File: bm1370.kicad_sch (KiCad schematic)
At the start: 48 parts, among them U5 MCP1824T-1202E/OT, U6 MCP1824T-0802E, U7 25MHz, U8 BM1370_mode1, U9 SN74AVC4T774

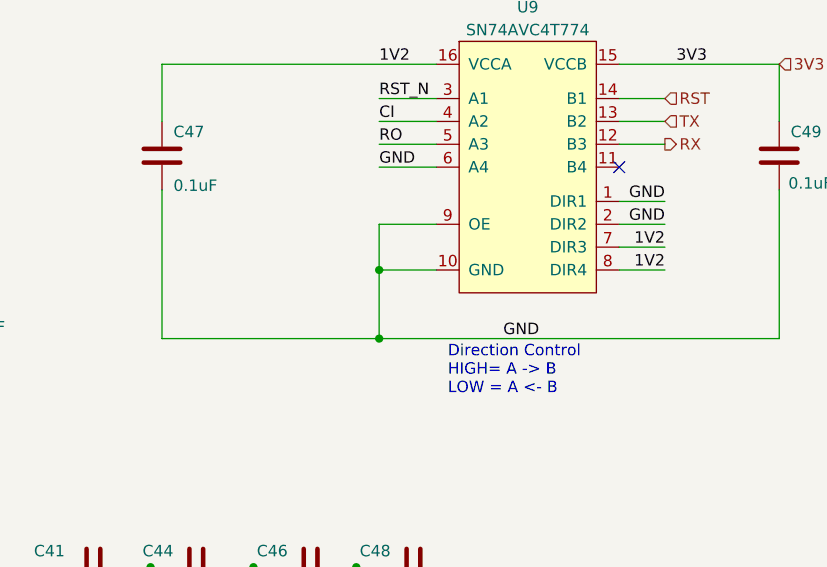
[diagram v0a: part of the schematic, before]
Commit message: Revert "bump version to 602. remove R21 and fix for #6"
This reverts commit 8bd74c865f9910776743c8aa45b35babe35214af.
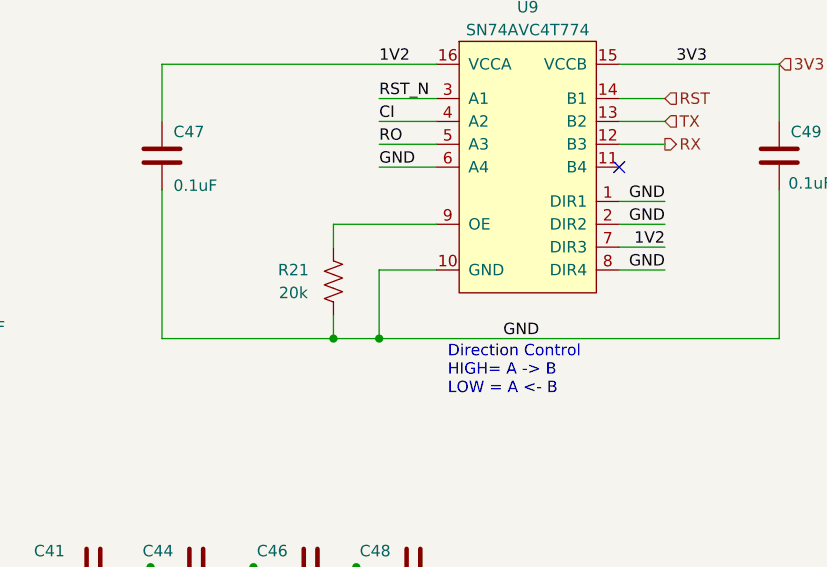
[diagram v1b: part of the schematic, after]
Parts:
- added R21: 20k, Resistor_SMD:R_0402_1005Metric, symbol Device:R_US
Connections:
- net 1V2: no longer U9.8 (DIR4)
- net GND: now also U9.8 (DIR4), R21.1; no longer U9.9 (OE)
- new net: R21.2, U9.9 (OE)
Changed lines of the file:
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@@
 	(title_block
 		(title "bitaxeGamma")
-		(date "2024-09-26")
-		(rev "602")
+		(date "2024-08-16")
+		(rev "600")
 	)
 	(junction
@@
 	)
 	(junction
-		(at 198.12 52.07)
-		(diameter 0)
-		(color 0 0 0 0)
-	)
-	(junction
 		(at 198.12 59.69)
 		(diameter 0)
@@
 	)
 	(junction
+		(at 193.04 59.69)
+		(diameter 0)
+		(color 0 0 0 0)
+	)
+	(junction
 		(at 140.97 85.09)
 		(diameter 0)
@@
 	(wire
 		(pts
-			(xy 242.57 43.18) (xy 242.57 59.69)
+			(xy 193.04 59.69) (xy 193.04 57.15)
 		)
 		(stroke
@@
 	(wire
 		(pts
-			(xy 180.34 127) (xy 180.34 133.35)
+			(xy 242.57 43.18) (xy 242.57 59.69)
 		)
 		(stroke
@@
 	(wire
 		(pts
-			(xy 64.77 43.18) (xy 60.96 43.18)
+			(xy 180.34 127) (xy 180.34 133.35)
 		)
 		(stroke
 			(width 0)
-			(type solid)
+			(type default)
 		)
 	)
 	(wire
 		(pts
-			(xy 31.75 66.04) (xy 31.75 69.85)
+			(xy 64.77 43.18) (xy 60.96 43.18)
 		)
 		(stroke
 			(width 0)
-			(type default)
+			(type solid)
 		)
 	)
 	(wire
 		(pts
-			(xy 158.75 109.22) (xy 171.45 109.22)
+			(xy 31.75 66.04) (xy 31.75 69.85)
 		)
 		(stroke
@@
 	(wire
 		(pts
-			(xy 204.47 46.99) (xy 198.12 46.99)
+			(xy 158.75 109.22) (xy 171.45 109.22)
 		)
 		(stroke
@@
 	(wire
 		(pts
+			(xy 193.04 46.99) (xy 193.04 49.53)
+		)
+		(stroke
+			(width 0)
+			(type default)
+		)
+	)
+	(wire
+		(pts
 			(xy 224.79 46.99) (xy 229.87 46.99)
 		)
@@
 	(wire
 		(pts
+			(xy 204.47 46.99) (xy 193.04 46.99)
+		)
+		(stroke
+			(width 0)
+			(type default)
+		)
+	)
+	(wire
+		(pts
 			(xy 105.41 53.34) (xy 105.41 50.8)
 		)
@@
 	(wire
 		(pts
-			(xy 173.99 59.69) (xy 198.12 59.69)
+			(xy 173.99 59.69) (xy 193.04 59.69)
 		)
 		(stroke
@@
 	(wire
 		(pts
-			(xy 198.12 46.99) (xy 198.12 52.07)
+			(xy 170.18 146.05) (xy 180.34 146.05)
 		)
 		(stroke
@@
 	(wire
 		(pts
-			(xy 170.18 146.05) (xy 180.34 146.05)
+			(xy 140.97 85.09) (xy 140.97 88.9)
 		)
 		(stroke
@@
 	(wire
 		(pts
-			(xy 140.97 85.09) (xy 140.97 88.9)
+			(xy 113.03 85.09) (xy 113.03 93.98)
 		)
 		(stroke
@@
 	(wire
 		(pts
-			(xy 113.03 85.09) (xy 113.03 93.98)
+			(xy 140.97 146.05) (xy 170.18 146.05)
 		)
 		(stroke
@@
 	(wire
 		(pts
-			(xy 140.97 146.05) (xy 170.18 146.05)
+			(xy 198.12 59.69) (xy 193.04 59.69)
 		)
 		(stroke
@@
 		)
 	)
+	(label "GND"
+		(at 229.87 52.07 180)
+		(fields_autoplaced yes)
+		(effects
+			(font
+				(size 1.27 1.27)
+			)
+			(justify right bottom)
+		)
+	)
 	(label "PIN_MODE"
 		(at 215.9 121.92 0)
@@
 		)
 	)
-	(label "1V2"
-		(at 229.87 52.07 180)
-		(fields_autoplaced yes)
-		(effects
-			(font
-				(size 1.27 1.27)
-			)
-			(justify right bottom)
-		)
-	)
 	(label "VDD3_1"
 		(at 171.45 99.06 180)
@@
 					(unit 1)
 				)
+			)
+		)
+	)
+	(symbol
+		(lib_id "Device:R_US")
+		(at 193.04 53.34 180)
+		(unit 1)
+		(exclude_from_sim no)
+		(in_bom yes)
+		(on_board yes)
+		(dnp no)
+		(property "Reference" "R21"
+			(at 188.595 52.07 0)
+			(effects
+				(font
+					(size 1.27 1.27)
+				)
+			)
+		)
+		(property "Value" "20k"
+			(at 188.595 54.61 0)
+			(effects
+				(font
+					(size 1.27 1.27)
+				)
+			)
+		)
+		(property "Footprint" "Resistor_SMD:R_0402_1005Metric"
+			(at 192.024 53.086 90)
+			(effects
+				(font
+					(size 1.27 1.27)
+				)
+				(hide yes)
+			)
+		)
+		(property "Datasheet" "~"
+			(at 193.04 53.34 0)
+			(effects
+				(font
+					(size 1.27 1.27)
+				)
+				(hide yes)
+			)
+		)
+		(property "Description" ""
+			(at 193.04 53.34 0)
+			(effects
+				(font
+					(size 1.27 1.27)
+				)
+				(hide yes)
+			)
+		)
+		(property "DK" "311-20.0KLRCT-ND"
+			(at 193.04 53.34 0)
+			(effects
+				(font
+					(size 1.27 1.27)
+				)
+				(hide yes)
+			)
+		)
+		(property "PARTNO" "RC0402FR-0720KL"
+			(at 193.04 53.34 0)
+			(effects
+				(font
+					(size 1.27 1.27)
+				)
+				(hide yes)
+			)
+		)
+		(pin "1"
+		)
+		(pin "2"
+		)
+		(instances
+			(project "bitaxeGamma"
+				(path "/e63e39d7-6ac0-4ffd-8aa3-1841a4541b55/4cf9c075-d009-4c35-9949-adda70ae20c7"
+					(reference "R21")
+					(unit 1)
+				)
